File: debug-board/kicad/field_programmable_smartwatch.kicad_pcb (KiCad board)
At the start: 4 copper layers, 22.5 x 31.5 mm, 30 parts, among them IC2 STM32WB55CEU6, J1 GPIO Header 1, J2 DX07S016JA1R1500, J3 GPIO Header 2, J4 SWD Header, SW2 SW_Push, Y1 32M, Y2 32.768k

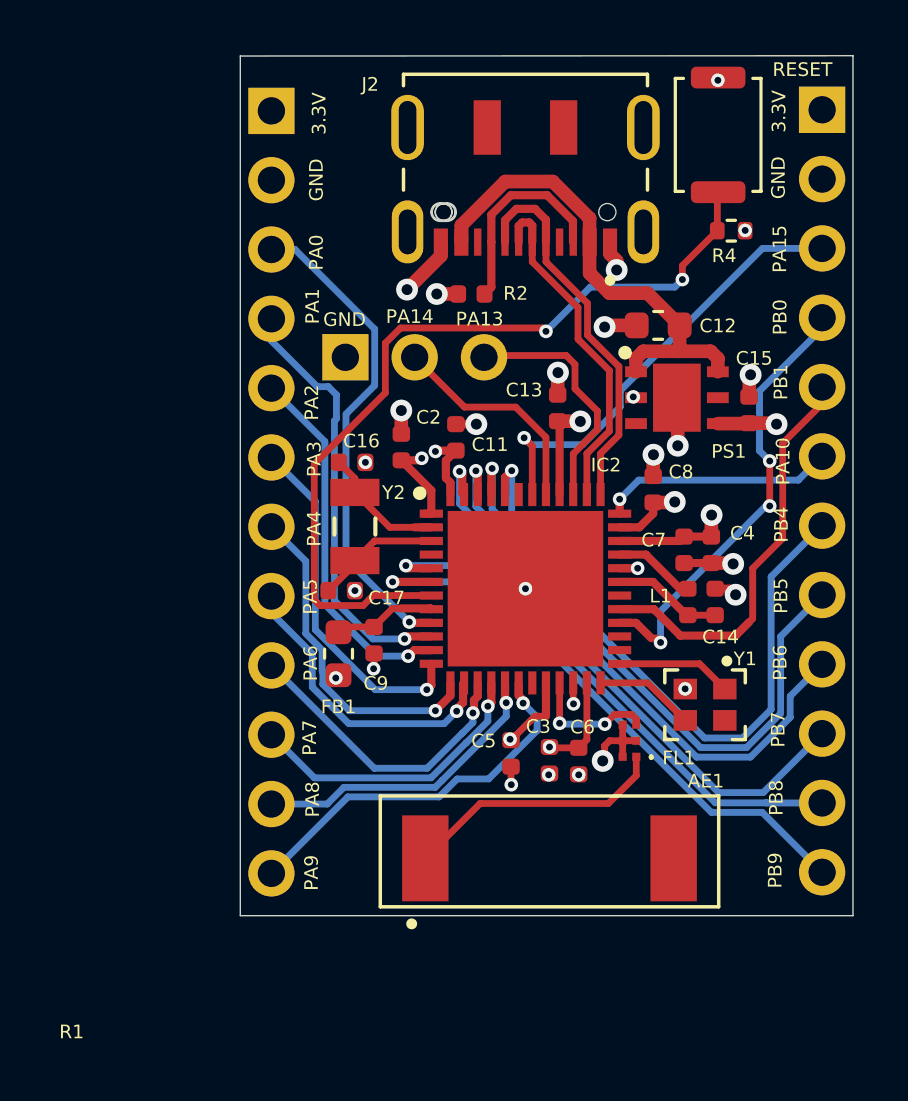
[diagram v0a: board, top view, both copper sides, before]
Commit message: Bring back the boot0 pin button
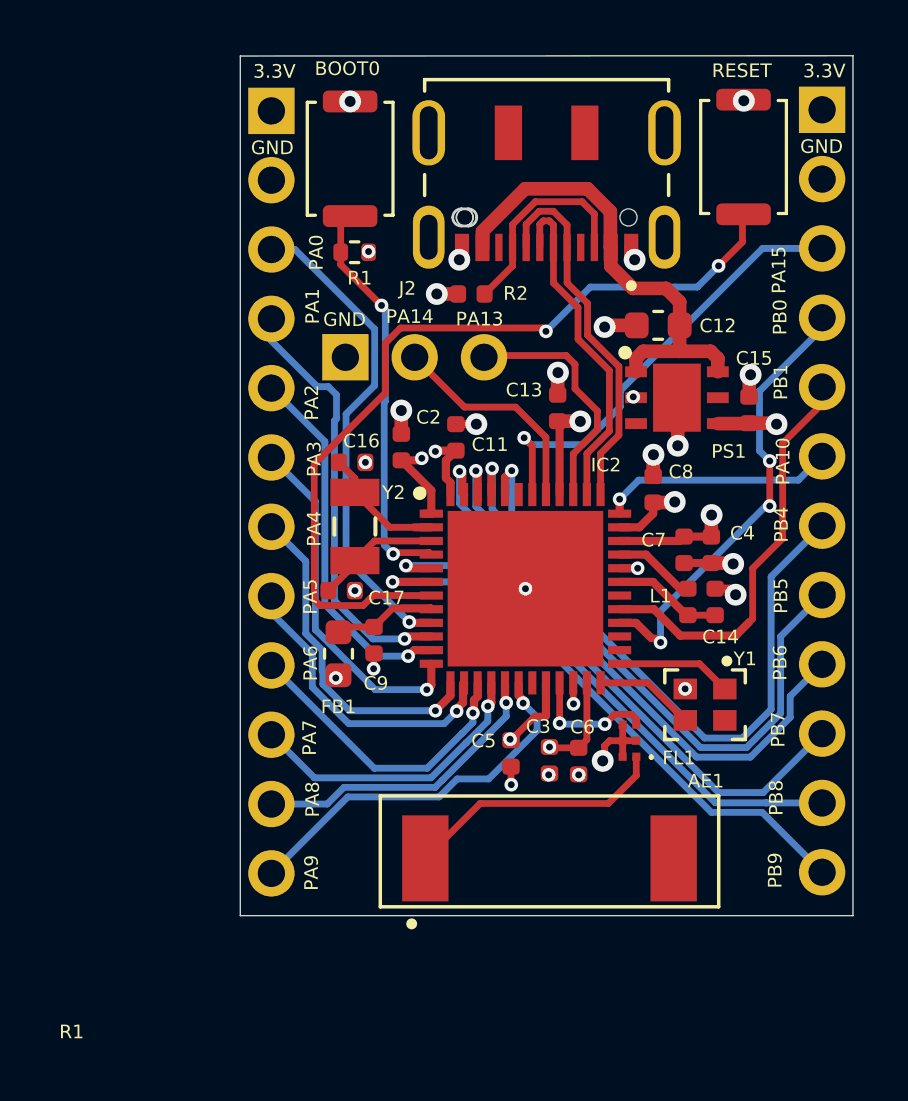
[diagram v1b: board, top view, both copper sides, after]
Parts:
- removed R4: 100k, Resistor_SMD:R_0402_1005Metric
- added R1: 100k, Resistor_SMD:R_0402_1005Metric, F.Cu at (158.8, 69.7)
- added SW1: SW_Push, Button_Switch_SMD:SW_Push_SPST_NO_Alps_SKRK, F.Cu at (158.6, 66.3)
- moved SW2 1.23 mm to (173.0, 66.2)
- moved J2 0.80 mm to (165.8, 68.4)
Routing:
- net /BOOT0: track 0.00 -> 14.8 mm, vias 0 -> 2
- net GND: track 19.9 -> 17.5 mm, vias 25 -> 26
- net /VBUS: track 18.1 -> 17.4 mm
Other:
- board text added: "BOOT0"
- board text removed: "R4"
